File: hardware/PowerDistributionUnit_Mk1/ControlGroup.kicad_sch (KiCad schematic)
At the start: 16 parts, among them U8 SN74AHC594QPWRQ1

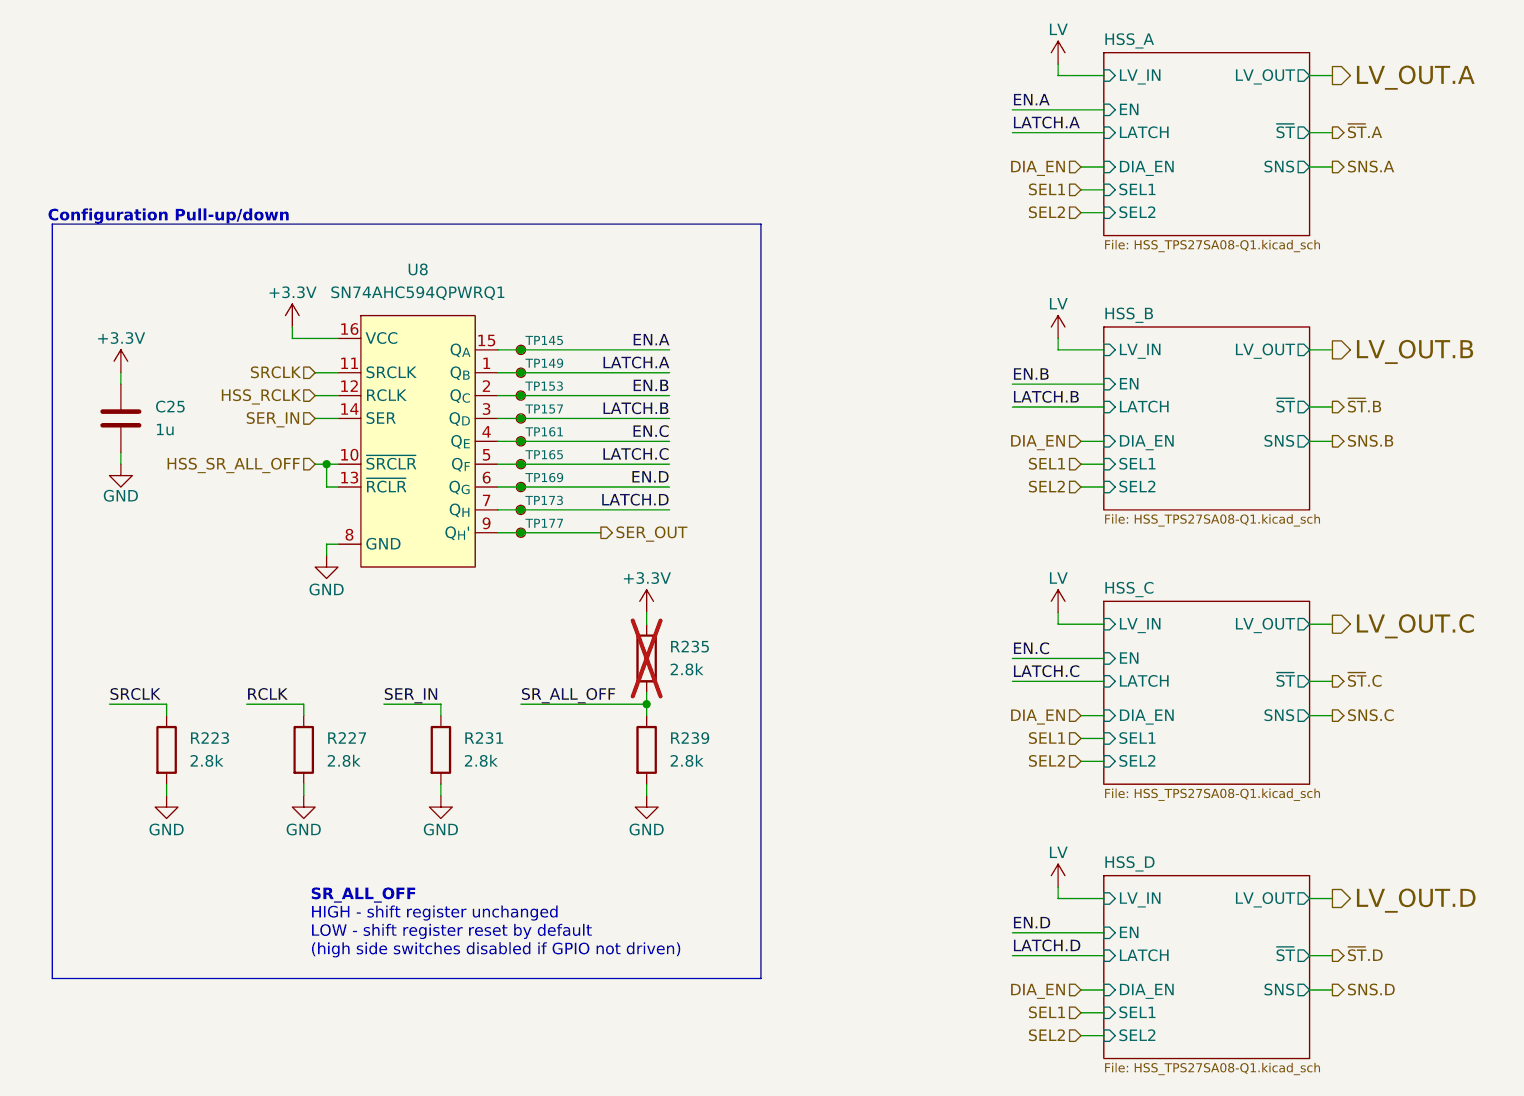
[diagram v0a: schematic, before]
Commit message: schematic updates (found switch, LED resistor values, LV sense ADC pin filter, removed unnecessary parallel resistors, switched to new SR), addressed review comments (input fuse, 3.3V LED, SPI naming fix)
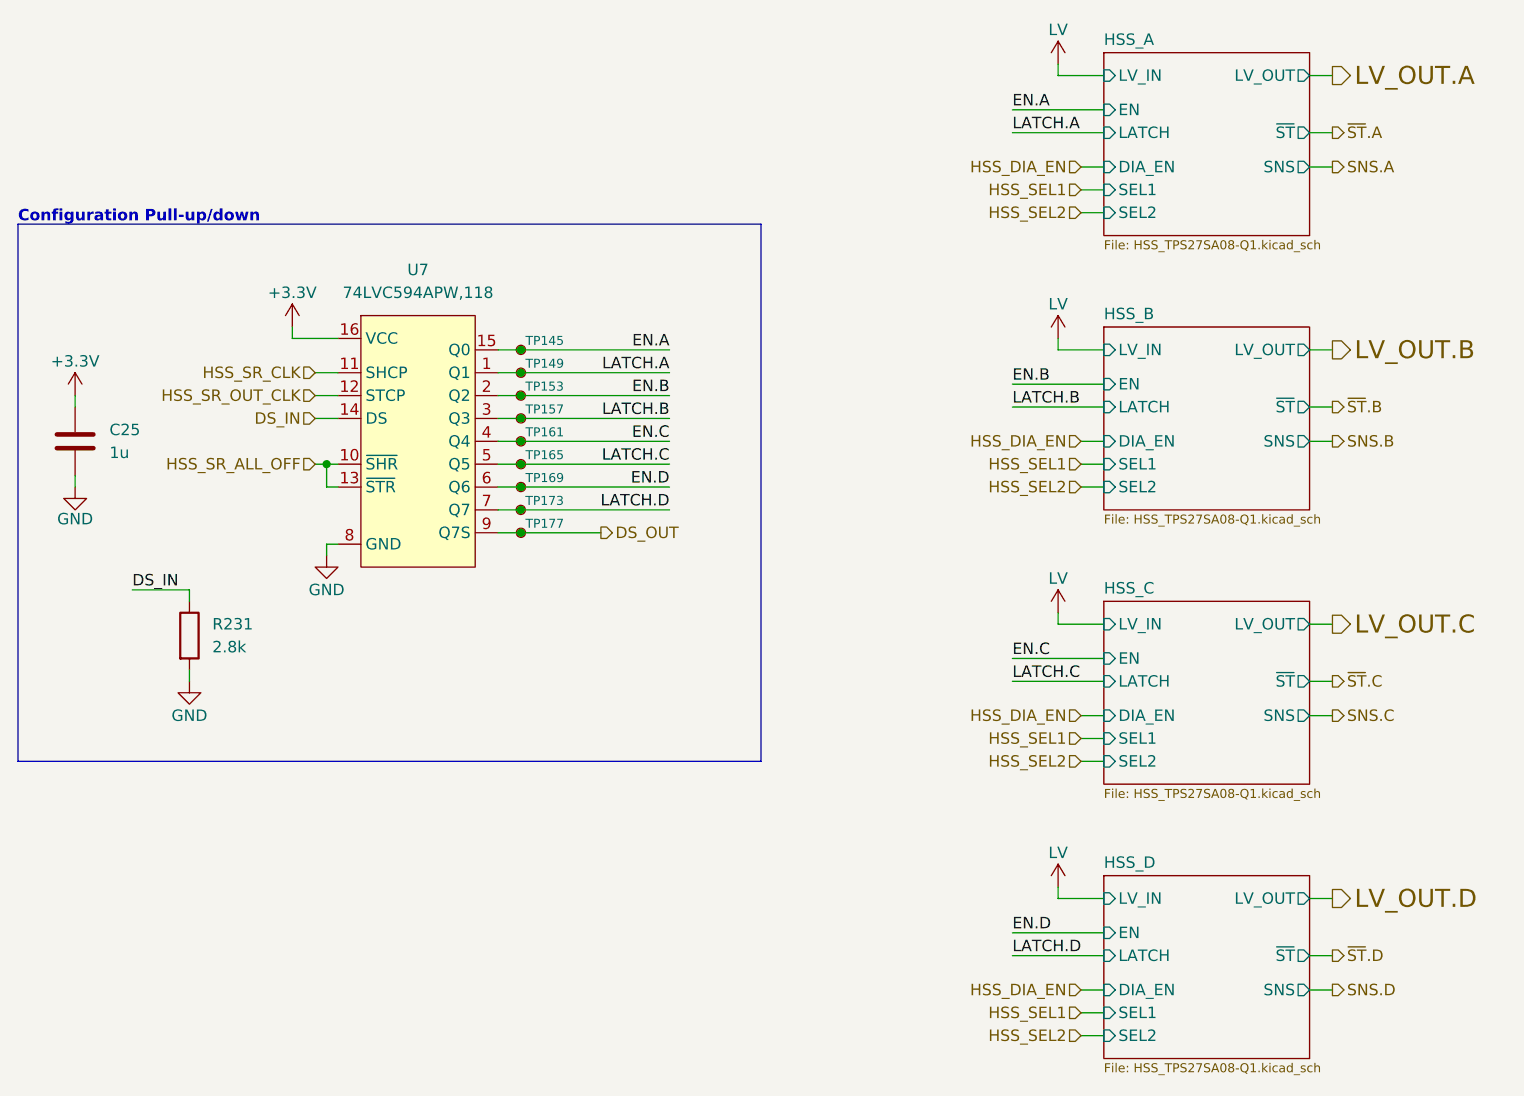
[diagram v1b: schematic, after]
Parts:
- removed R223, R227, R235, R239: 2.8k, Resistor_SMD:R_0603_1608Metric, symbol PowerDistributionUnitResistorLib:2.8k
- removed U8: SN74AHC594QPWRQ1, Package_SO:TSSOP-16_4.4x5mm_P0.65mm, symbol PowerDistributionUnitLib:SN74AHC594QPWRQ1
- added U7: 74LVC594APW,118, Package_SO:SOIC-16_3.9x9.9mm_P1.27mm, symbol PowerDistributionUnitLib:74LVC594APW,118
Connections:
- net +3.3V: now also U7.16 (VCC)
- net EN.A: now also U7.15 (Q0)
- net EN.B: now also U7.2 (Q2)
- net EN.C: now also U7.4 (Q4)
- net EN.D: now also U7.6 (Q6)
- net GND: now also U7.8 (GND)
- net HSS_SR_ALL_OFF: now also U7.10 (~{SHR}), U7.13 (~{STR})
- net LATCH.A: now also U7.1 (Q1)
- net LATCH.B: now also U7.3 (Q3)
- net LATCH.C: now also U7.5 (Q5)
- net LATCH.D: now also U7.7 (Q7)
- net SER_IN renamed DS_IN
- net DS_IN: now also U7.14 (DS)
- net SER_OUT renamed DS_OUT
- net DS_OUT: now also U7.9 (Q7S)
- new net HSS_SR_CLK: U7.11 (SHCP)
- new net HSS_SR_OUT_CLK: U7.12 (STCP)
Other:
- note removed: "HIGH - shift register unchanged LOW - shift register reset by default (high side switches disabled if GPIO not driven)"
- note removed: "SR_ALL_OFF"
- moved on the sheet: C25, R231

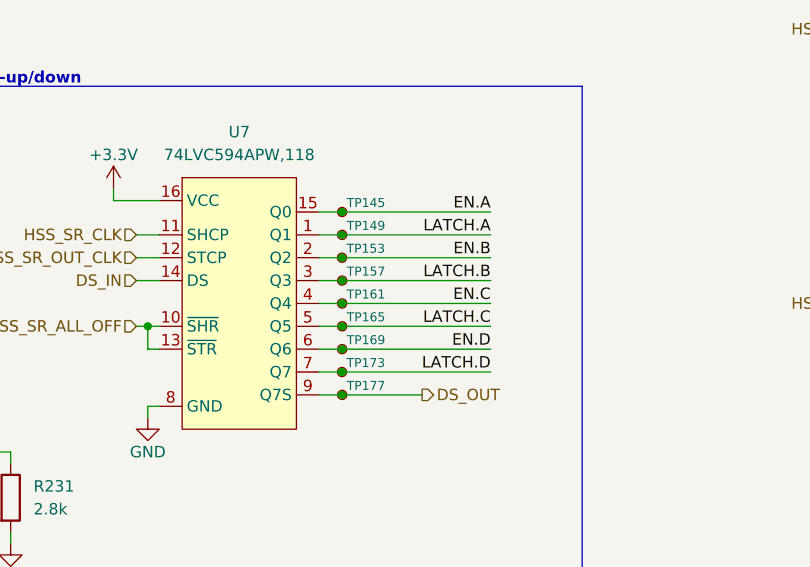
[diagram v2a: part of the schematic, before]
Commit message: one side HSS routing
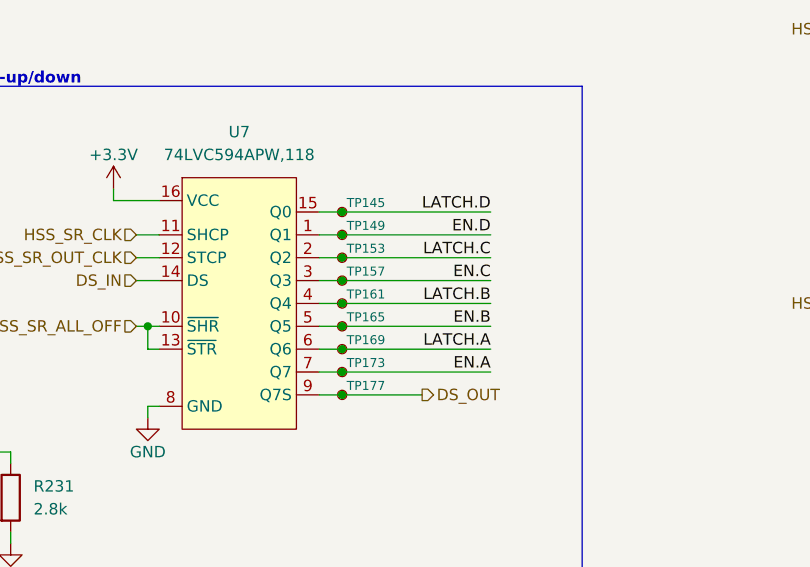
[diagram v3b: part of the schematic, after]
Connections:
- net EN.A: now also TP173.1, U7.7 (Q7); no longer TP145.1, U7.15 (Q0)
- net EN.B: now also TP165.1, U7.5 (Q5); no longer TP153.1, U7.2 (Q2)
- net EN.C: now also TP157.1, U7.3 (Q3); no longer TP161.1, U7.4 (Q4)
- net EN.D: now also TP149.1, U7.1 (Q1); no longer TP169.1, U7.6 (Q6)
- net LATCH.A: now also TP169.1, U7.6 (Q6); no longer TP149.1, U7.1 (Q1)
- net LATCH.B: now also TP161.1, U7.4 (Q4); no longer TP157.1, U7.3 (Q3)
- net LATCH.C: now also TP153.1, U7.2 (Q2); no longer TP165.1, U7.5 (Q5)
- net LATCH.D: now also TP145.1, U7.15 (Q0); no longer TP173.1, U7.7 (Q7)

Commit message: update all symbols with LCSC P/N
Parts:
- C25: LCSC P/N (none) -> C15849
- R231: LCSC P/N (none) -> C844548
- U7: LCSC P/N (none) -> C548830
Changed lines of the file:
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@@
+			)
+		)
+		(property "LCSC P/N" "C844548"
+			(at 64.77 102.87 0)
+			(effects
+				(font
+					(size 1.27 1.27)
+				)
+				(hide yes)
 			)
 		)
@@
 		)
 		(property "Digikey P/N" "1727-6687-1-ND"
+			(at 90.17 81.28 0)
+			(effects
+				(font
+					(size 1.27 1.27)
+				)
+				(hide yes)
+			)
+		)
+		(property "LCSC P/N" "C548830"
 			(at 90.17 81.28 0)
 			(effects
@@
 			(at 52.07 81.28 0)
 			(effects
+				(font
+					(size 1.27 1.27)
+				)
+				(hide yes)
+			)
+		)
+		(property "LCSC P/N" "C15849"
+			(at 52.07 81.28 0)
+			(effects

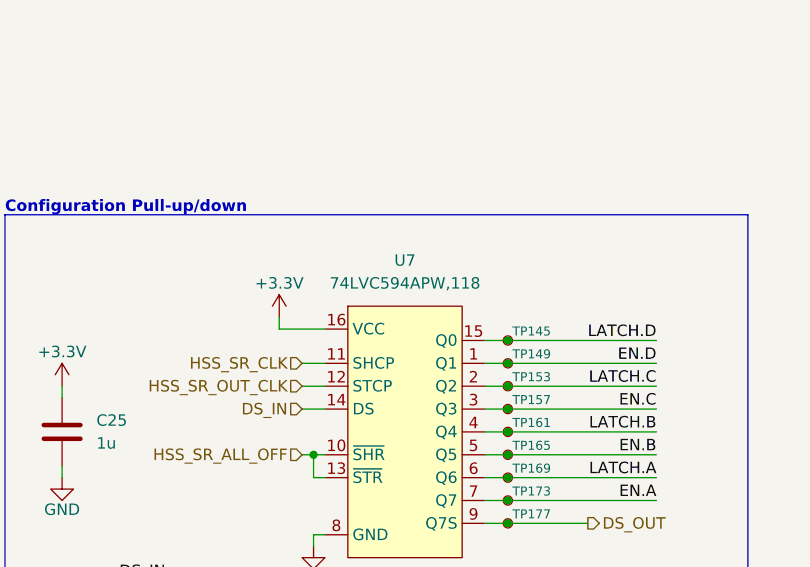
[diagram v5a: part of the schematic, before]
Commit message: correct SR part number to SOIC package
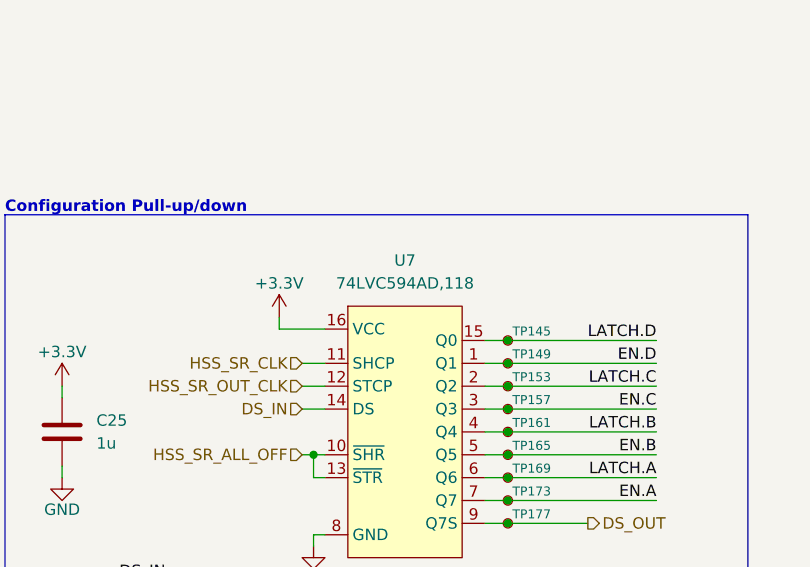
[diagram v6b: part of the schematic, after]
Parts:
- U7: value 74LVC594APW,118 -> 74LVC594AD,118; symbol PowerDistributionUnitLib:74LVC594APW,118 -> PowerDistributionUnitLib:74LVC594AD,118; Digikey P/N 1727-6687-1-ND -> 1727-74LVC594AD,118CT-ND; LCSC P/N C548830 -> C548827; Mouser P/N 771-LVC594APW118 -> 771-LVC594AD118; P/N 74LVC594APW,118 -> 74LVC594AD,118
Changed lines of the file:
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@@
 	)
 	(symbol
-		(lib_id "PowerDistributionUnitLib:74LVC594APW,118")
+		(lib_id "PowerDistributionUnitLib:74LVC594AD,118")
 		(at 90.17 81.28 0)
 		(unit 1)
@@
 			)
 		)
-		(property "Value" "74LVC594APW,118"
+		(property "Value" "74LVC594AD,118"
 			(at 90.17 64.77 0)
 			(effects
@@
 			)
 		)
-		(property "P/N" "74LVC594APW,118"
+		(property "P/N" "74LVC594AD,118"
 			(at 90.17 81.28 0)
 			(effects
@@
 			)
 		)
-		(property "Mouser P/N" "771-LVC594APW118"
+		(property "Mouser P/N" "771-LVC594AD118"
 			(at 90.17 81.28 0)
 			(effects
@@
 			)
 		)
-		(property "Digikey P/N" "1727-6687-1-ND"
+		(property "Digikey P/N" "1727-74LVC594AD,118CT-ND"
 			(at 90.17 81.28 0)
 			(effects
@@
 			)
 		)
-		(property "LCSC P/N" "C548830"
+		(property "LCSC P/N" "C548827"
 			(at 90.17 81.28 0)
 			(effects

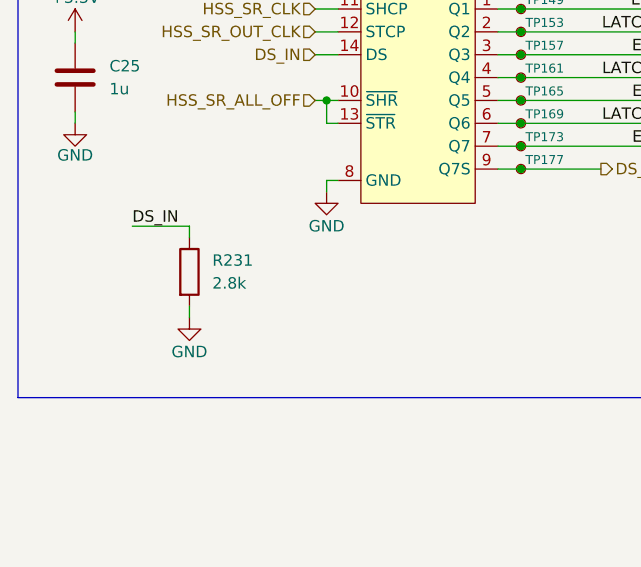
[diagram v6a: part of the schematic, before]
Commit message: change lv sense rdiv values to avoid extended components, update all pull-ups/-downs using 2.8k
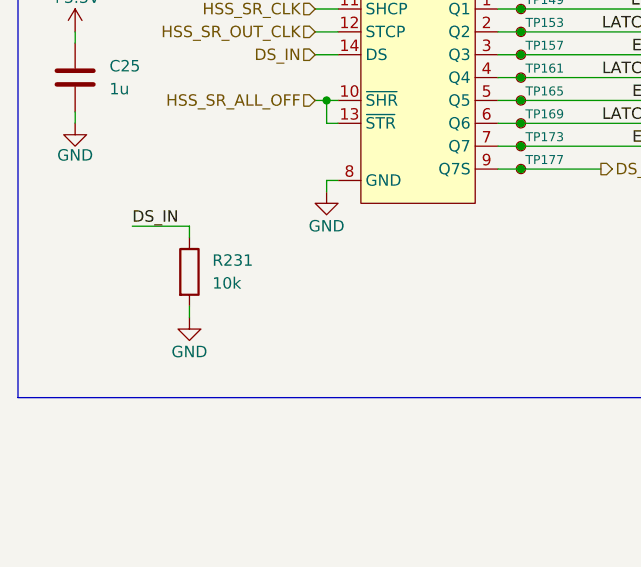
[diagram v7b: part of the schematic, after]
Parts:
- R231: value 2.8k -> 10k; symbol PowerDistributionUnitResistorLib:2.8k -> PowerDistributionUnitResistorLib:10k; LCSC P/N C844548 -> C25804; Mouser P/N 71-CRCW0603-2.8K-E3 -> 71-CRCW060310K0FKEI; P/N CRCW06032K80FKEA -> CRCW060310K0FKEI
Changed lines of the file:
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@@
 	)
 	(symbol
-		(lib_id "PowerDistributionUnitResistorLib:2.8k")
+		(lib_id "PowerDistributionUnitResistorLib:10k")
 		(at 64.77 102.87 0)
 		(unit 1)
@@
 			)
 		)
-		(property "Value" "2.8k"
+		(property "Value" "10k"
 			(at 67.31 104.1399 0)
 			(effects
@@
 			)
 		)
-		(property "P/N" "CRCW06032K80FKEA"
+		(property "P/N" "CRCW060310K0FKEI"
 			(at 64.77 102.87 0)
 			(effects
@@
 			)
 		)
-		(property "Mouser P/N" "71-CRCW0603-2.8K-E3"
+		(property "Mouser P/N" "71-CRCW060310K0FKEI"
 			(at 64.77 102.87 0)
 			(effects
@@
 			)
 		)
-		(property "LCSC P/N" "C844548"
+		(property "LCSC P/N" "C25804"
 			(at 64.77 102.87 0)
 			(effects
